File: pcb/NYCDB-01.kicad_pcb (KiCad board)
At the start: 2 copper layers, 264 parts, among them J1 AUDIO_JACK, P1 CONN_BATT, P2 USB_OTG, Q1 Q_PMOS_GSD, SW1 SW_POWER, SW2 SW_RESET, U1 CS5361, U10 OPA4134, U11 TPA6120A2, U12 24C16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

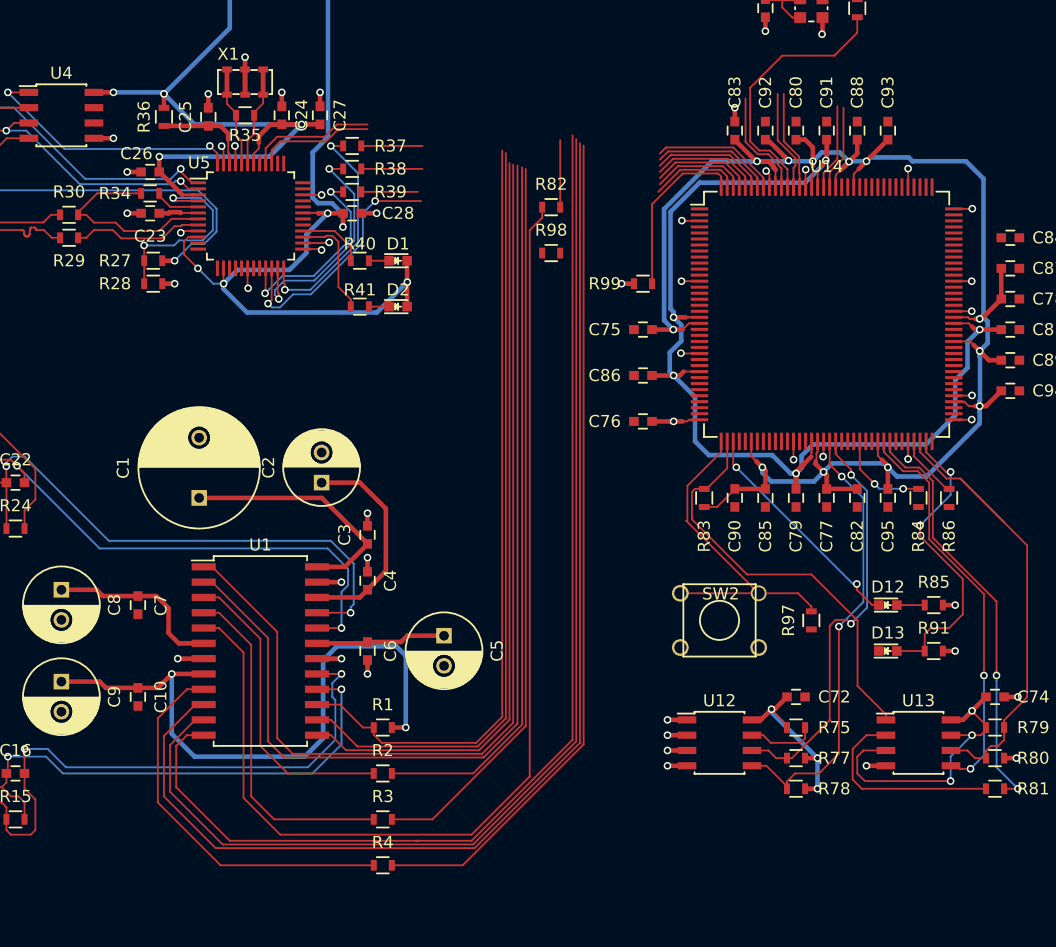
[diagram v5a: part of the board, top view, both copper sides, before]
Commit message: Reordering the ADC->FPGA pins for layout
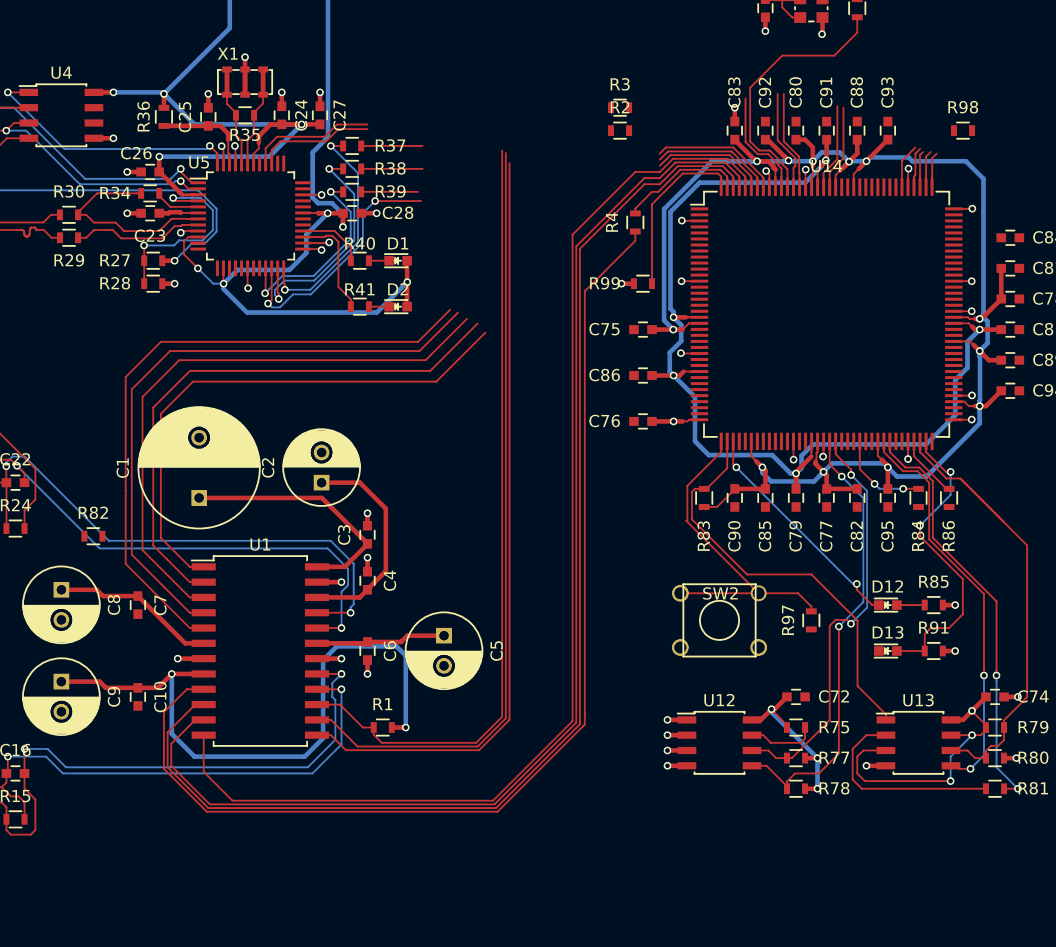
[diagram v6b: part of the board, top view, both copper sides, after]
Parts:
- moved R3 62.2 mm to (114.9, 85.7)
- moved R4 57.3 mm to (116.2, 95.2), turned to 90 degrees
- moved R2 56.9 mm to (114.9, 87.6)
- moved R82 46.8 mm to (71.2, 121.3)
- moved R98 35.7 mm to (143.4, 87.6)
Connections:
- U14 pad 126: /CS5361 ADC/ADC_SDO -> /CS5361 ADC/ADC_RST
- U14 pad 134: /CS5361 ADC/ADC_MDIV -> /CS5361 ADC/ADC_OVFL
- U14 pad 139: /CS5361 ADC/ADC_HPF -> /CS5361 ADC/ADC_MS
- U14 pad 140: /CS5361 ADC/ADC_MS -> /CS5361 ADC/ADC_I2S_LJ
- U14 pad 141: /CS5361 ADC/ADC_I2S_LJ -> /CS5361 ADC/ADC_HPF
- U14 pad 142: /CS5361 ADC/ADC_OVFL -> /CS5361 ADC/ADC_MDIV
- U14 pad 143: /CS5361 ADC/ADC_RST -> /CS5361 ADC/ADC_SDO
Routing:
- net /CS5361 ADC/ADC_SDO: track 76.8 -> 10.5 mm
- net /CS5361 ADC/ADC_SCLK: track 68.8 -> 8.28 mm
- net Net-(R4-Pad1): track 31.9 -> 91.0 mm
- net /CS5361 ADC/ADC_LRCLK: track 65.9 -> 7.19 mm
- net /CS5361 ADC/ADC_RST: track 92.2 -> 52.3 mm
- net /CS5361 ADC/ADC_MCLK: track 90.9 -> 53.4 mm
- net /CS5361 ADC/ADC_MS: track 93.6 -> 57.0 mm
- net Net-(R2-Pad1): track 25.4 -> 49.0 mm
- net Net-(R3-Pad1): track 28.6 -> 51.4 mm
- net /CS5361 ADC/ADC_I2S_LJ: track 103.1 -> 96.2 mm
- net /CS5361 ADC/ADC_MDIV: track 108.2 -> 101.6 mm
- net /CS5361 ADC/ADC_HPF: track 106.1 -> 100.4 mm
- net Net-(R82-Pad1): track 14.0 -> 8.41 mm
- net /FT2232D/USB_TXD: track 10.5 -> 14.3 mm
- net /FT2232D/USB_RXD: track 9.79 -> 13.2 mm
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
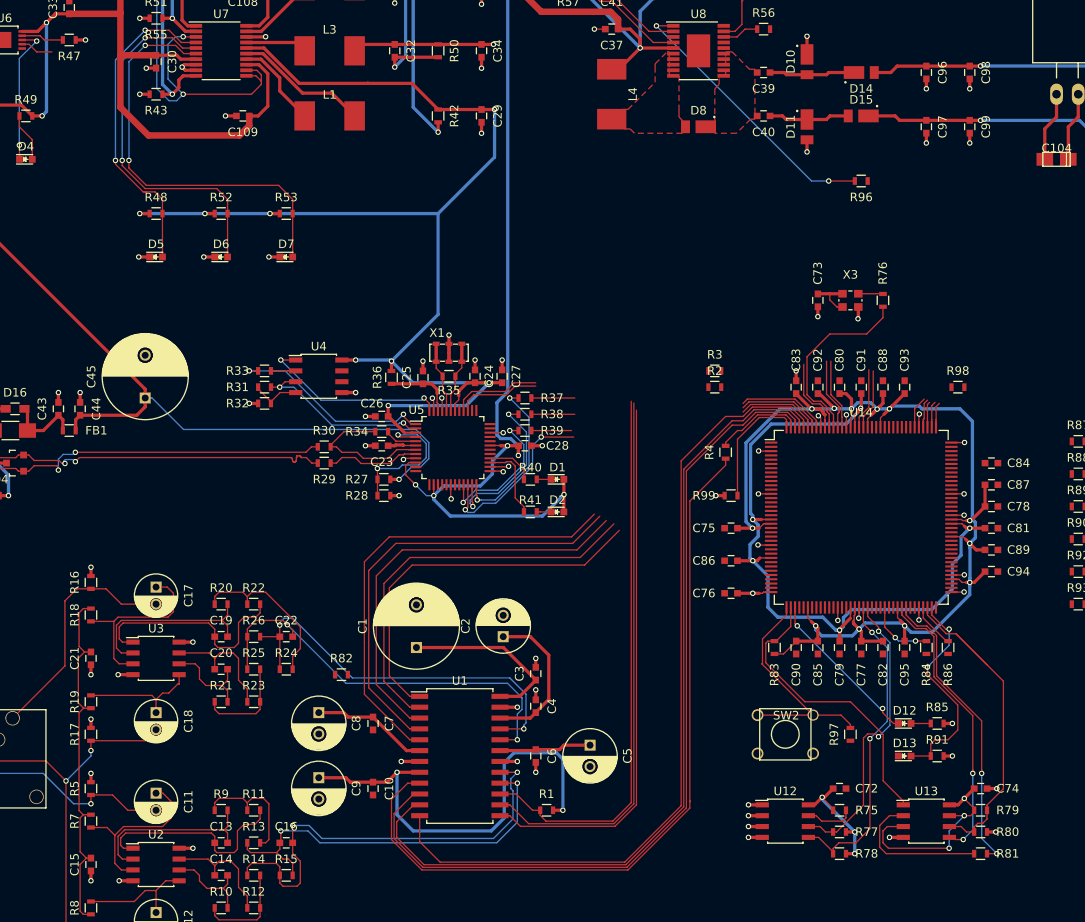
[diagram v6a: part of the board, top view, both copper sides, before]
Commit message: Finished pin swapping the FPGA ADC signals
Still not super jazzed about how coupled the ADC I2S traces are, and I
need to look into the MCLK situation for the ADC.  Ideally the FPGA
shouldn't be generating it since it's a lousy clock driver.  Will
probably need another oscillator for the ADC same as the FPGA and DAC.
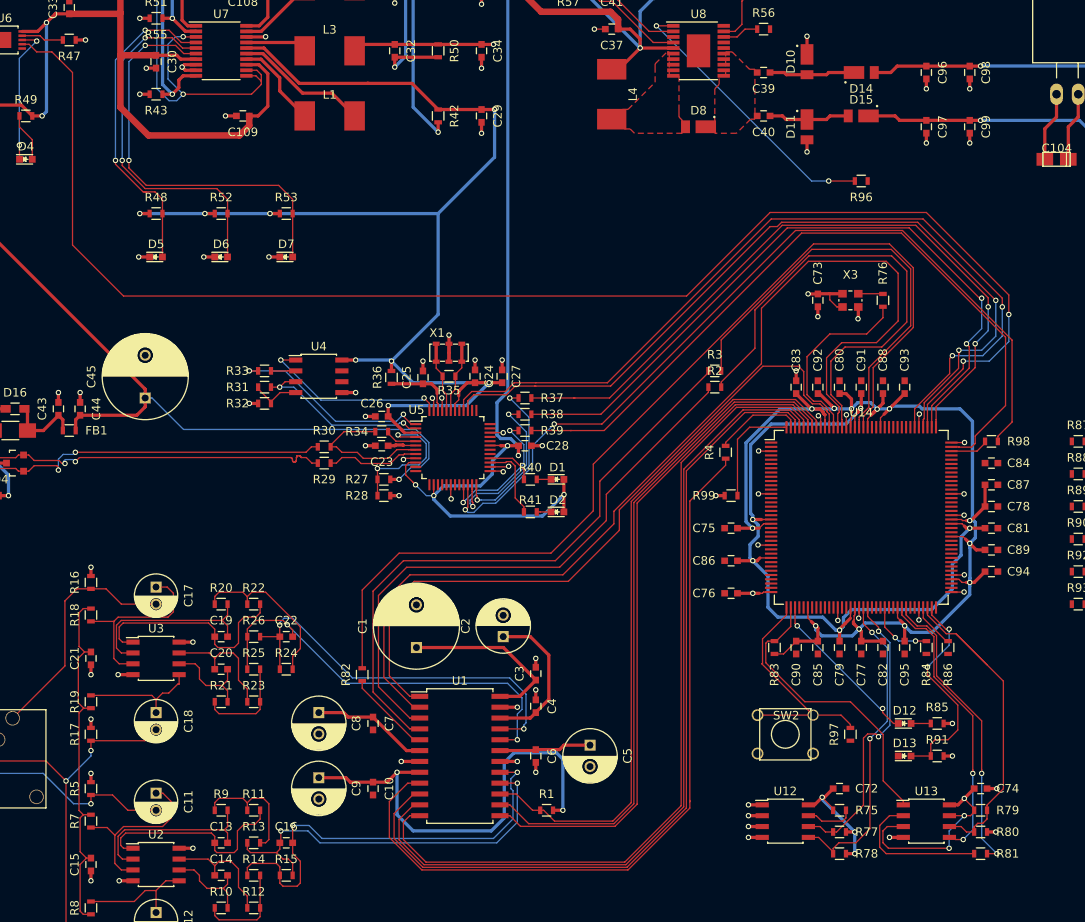
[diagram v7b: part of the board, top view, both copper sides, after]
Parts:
- moved R98 7.47 mm to (147.3, 94.0), turned to 0 degrees
- moved R82 2.42 mm to (73.7, 121.3), turned to 270 degrees
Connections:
- U14 pad 126: /CS5361 ADC/ADC_RST -> Net-(R82-Pad1)
- U14 pad 127: /CS5361 ADC/ADC_LRCLK -> /CS5361 ADC/ADC_SCLK
- U14 pad 131: /CS5361 ADC/ADC_SCLK -> /CS5361 ADC/ADC_LRCLK
- U14 pad 132: Net-(R82-Pad1) -> /CS5361 ADC/ADC_MS
- U14 pad 134: /CS5361 ADC/ADC_OVFL -> /CS5361 ADC/ADC_RST
- U14 pad 137: /CS5361 ADC/ADC_M1 -> /CS5361 ADC/ADC_OVFL
- U14 pad 138: /CS5361 ADC/ADC_M0 -> /CS5361 ADC/ADC_M1
- U14 pad 139: /CS5361 ADC/ADC_MS -> /CS5361 ADC/ADC_M0
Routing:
- net /Power Supplies/ISET2: track 6.87 -> 168.8 mm, vias 0 -> 2
- net Net-(R82-Pad1): track 8.41 -> 115.9 mm
- net /FT2232D/USB_TXD: track 14.3 -> 98.4 mm, vias 0 -> 2
- net /FT2232D/TMS: track 4.71 -> 87.2 mm
- net /FT2232D/USB_RXD: track 13.2 -> 95.4 mm, vias 0 -> 2
- net /FT2232D/TDO: track 20.9 -> 100.1 mm
- net /FT2232D/TCK: track 8.04 -> 83.2 mm, vias 0 -> 2
- net /FT2232D/TDI: track 8.16 -> 83.0 mm, vias 0 -> 2
- net /CS5361 ADC/ADC_MS: track 57.0 -> 121.7 mm
- net /CS5361 ADC/ADC_LRCLK: track 7.19 -> 56.8 mm
- net /CS5361 ADC/ADC_SCLK: track 8.28 -> 52.2 mm
- net /CS5361 ADC/ADC_MCLK: track 53.4 -> 10.1 mm
- net /CS5361 ADC/ADC_RST: track 52.3 -> 83.5 mm
- net Net-(R3-Pad1): track 51.4 -> 71.5 mm
- net Net-(R2-Pad1): track 49.0 -> 67.9 mm
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
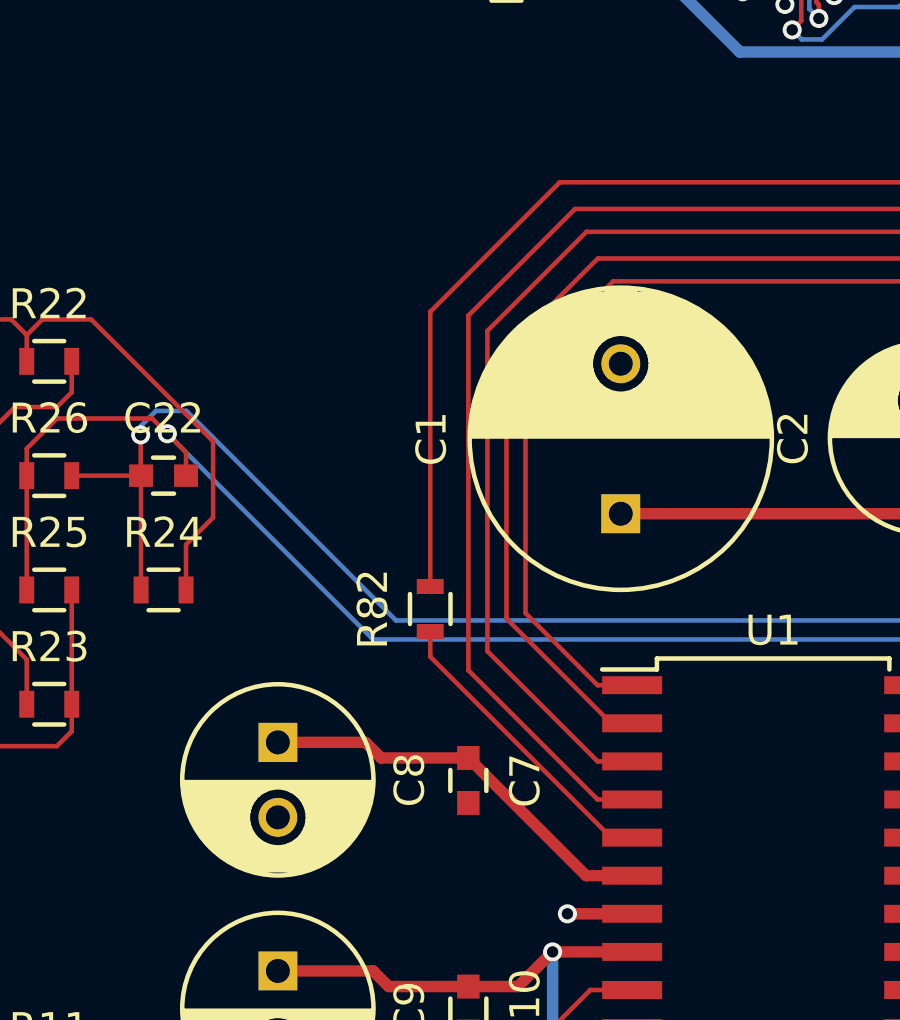
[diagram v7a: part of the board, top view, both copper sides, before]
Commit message: Added an oscillator for the ADC
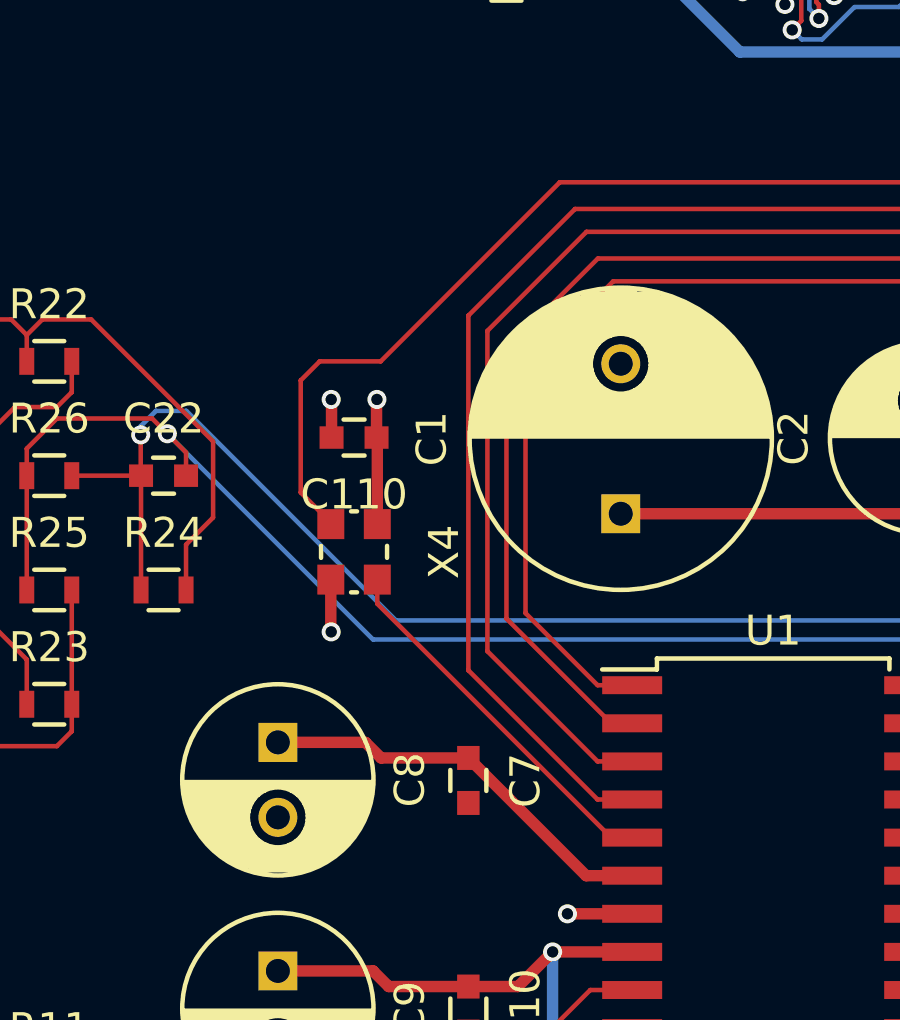
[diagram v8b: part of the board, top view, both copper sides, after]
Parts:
- removed R82: 68, Resistors_SMD:R_0603
- added C110: 0.1uF, Capacitors_SMD:C_0603, F.Cu at (71.1, 115.6)
- added X4: 12.288MHz, headphones:Oscillator_SMD_2520_4Pads, F.Cu at (71.1, 119.4)
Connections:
- U1 pad 5: /CS5361 ADC/ADC_MCLK -> Net-(U1-Pad5)
- U14 pad 126: Net-(R82-Pad1) -> /CS5361 ADC/ADC_MCLK_EN
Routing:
- net /CS5361 ADC/ADC_MCLK_EN: track 0.00 -> 117.2 mm
- net Net-(R82-Pad1): track 115.9 -> 0.00 mm
- net Net-(U1-Pad5): track 0.00 -> 12.5 mm
- net /CS5361 ADC/ADC_MCLK: track 10.1 -> 0.00 mm
- net +3V3: track 393.3 -> 397.5 mm, vias 31 -> 32
- net GND: track 138.2 -> 141.2 mm, vias 84 -> 86
